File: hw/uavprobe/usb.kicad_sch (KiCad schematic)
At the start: 50 parts, among them J1 USB_C_Receptacle_USB2.0_14P, SW2 Reset, U6 NCP1117-5.0_SOT223, U7 TPS2561, U8 USB2412-DZK, Y2 24MHz

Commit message: AISLER-friendly BOM fields
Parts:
- J1: MPN USB4105-GF-A -> USB4105-GF-A
- SW2: MPN SW_SPST_B3U-1000P -> B3U-1000PM
- TP6, TP7, TP8, TP9: now left out of the parts list
- U6: MPN NCP1117-5.0_SOT223 -> NCP1117ST33T3G
- U7: MPN TPS2561 -> TPS2561DRCT
- Y2: MPN ABM3B-24.000MHZ-10-B-1-U-T -> ABM3B-24.000MHZ-10-1-U-T
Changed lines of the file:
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@@
 			)
 		)
-		(property "MPN" "SW_SPST_B3U-1000P"
+		(property "MPN" "B3U-1000PM"
 			(at 160.02 144.78 0)
 			(effects
@@
 		(unit 1)
 		(exclude_from_sim no)
-		(in_bom yes)
+		(in_bom no)
 		(on_board yes)
 		(dnp no)
@@
 		(unit 1)
 		(exclude_from_sim no)
-		(in_bom yes)
+		(in_bom no)
 		(on_board yes)
 		(dnp no)
@@
 		(unit 1)
 		(exclude_from_sim no)
-		(in_bom yes)
+		(in_bom no)
 		(on_board yes)
 		(dnp no)
@@
 			)
 		)
-		(property "MPN" "NCP1117-5.0_SOT223"
+		(property "MPN" "NCP1117ST33T3G"
 			(at 90.17 130.81 0)
 			(effects
@@
 			)
 		)
-		(property "MPN" "TPS2561"
+		(property "MPN" "TPS2561DRCT"
 			(at 83.82 168.91 0)
 			(effects
@@
 			)
 		)
-		(property "MPN" "USB4105-GF-A"
+		(property "MPN" "USB4105-GF-A "
 			(at 38.1 71.12 0)
 			(effects
@@
 		(unit 1)
 		(exclude_from_sim no)
-		(in_bom yes)
+		(in_bom no)
 		(on_board yes)
 		(dnp no)
@@
 			)
 		)
-		(property "MPN" "ABM3B-24.000MHZ-10-B-1-U-T"
+		(property "MPN" "ABM3B-24.000MHZ-10-1-U-T"
 			(at 194.31 52.07 0)
 			(effects

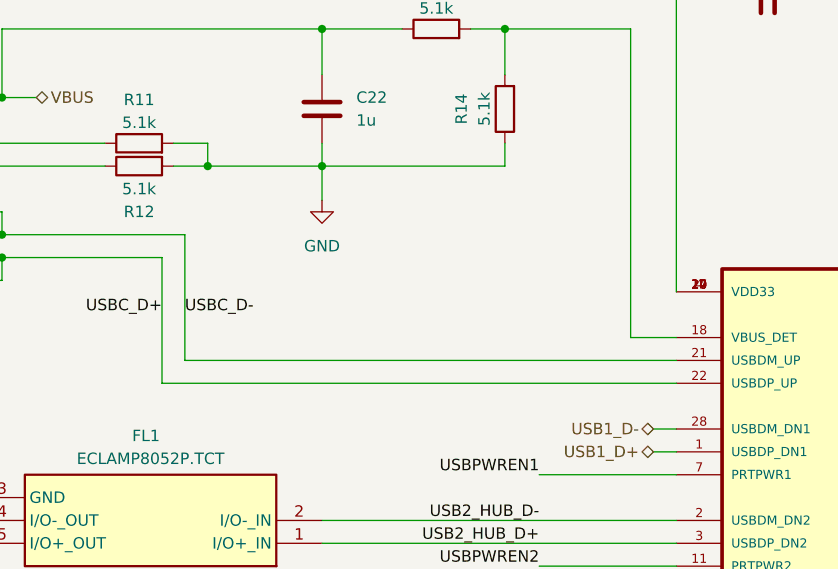
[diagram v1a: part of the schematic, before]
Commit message: Layout 2
Honoring the DRC and with a new uSB-C connector
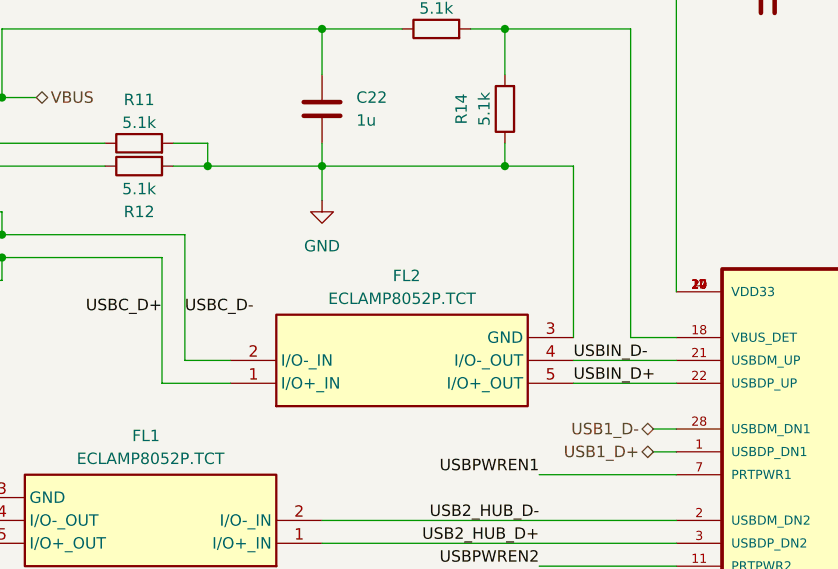
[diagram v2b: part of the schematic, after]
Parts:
- added FL2: ECLAMP8052P.TCT, Import:ECLAMP8052PTCT, symbol ECLAMP850:ECLAMP8052P.TCT
- J1: footprint Connector_USB:USB_C_Receptacle_GCT_USB4105-xx-A_16P_TopMnt_Horizontal -> Connector_USB:USB_C_Receptacle_Amphenol_124019772112A
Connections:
- net GND: now also FL2.3 (GND)
- net USBC_D+: now also FL2.1 (I/O+_IN); no longer U8.22 (USBDP_UP)
- net USBC_D-: now also FL2.2 (I/O-_IN); no longer U8.21 (USBDM_UP)
- new net USBIN_D+: FL2.5 (I/O+_OUT), U8.22 (USBDP_UP)
- new net USBIN_D-: FL2.4 (I/O-_OUT), U8.21 (USBDM_UP)
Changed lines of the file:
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@@
 	)
 	(junction
+		(at 114.3 63.5)
+		(diameter 0)
+		(color 0 0 0 0)
+	)
+	(junction
 		(at 110.49 149.86)
 		(diameter 0)
@@
 	(wire
 		(pts
+			(xy 121.92 85.09) (xy 133.35 85.09)
+		)
+		(stroke
+			(width 0)
+			(type default)
+		)
+	)
+	(wire
+		(pts
 			(xy 238.76 46.99) (xy 238.76 68.58)
 		)
@@
 	(wire
 		(pts
+			(xy 121.92 63.5) (xy 114.3 63.5)
+		)
+		(stroke
+			(width 0)
+			(type default)
+		)
+	)
+	(wire
+		(pts
 			(xy 199.39 67.31) (xy 199.39 77.47)
 		)
@@
 	(wire
 		(pts
-			(xy 252.73 116.84) (xy 261.62 116.84)
+			(xy 121.92 82.55) (xy 121.92 63.5)
 		)
 		(stroke
@@
 	(wire
 		(pts
-			(xy 53.34 63.5) (xy 69.85 63.5)
+			(xy 252.73 116.84) (xy 261.62 116.84)
 		)
 		(stroke
@@
 	(wire
 		(pts
-			(xy 210.82 44.45) (xy 210.82 57.15)
+			(xy 53.34 63.5) (xy 69.85 63.5)
 		)
 		(stroke
@@
 	(wire
 		(pts
-			(xy 93.98 60.96) (xy 93.98 63.5)
+			(xy 210.82 44.45) (xy 210.82 57.15)
 		)
 		(stroke
@@
 	(wire
 		(pts
-			(xy 114.3 63.5) (xy 114.3 60.96)
+			(xy 93.98 60.96) (xy 93.98 63.5)
 		)
 		(stroke
@@
 	(wire
 		(pts
-			(xy 110.49 158.75) (xy 123.19 158.75)
+			(xy 114.3 63.5) (xy 114.3 60.96)
 		)
 		(stroke
@@
 	(wire
 		(pts
-			(xy 133.35 85.09) (xy 78.74 85.09)
+			(xy 110.49 158.75) (xy 123.19 158.75)
 		)
 		(stroke
@@
 	(wire
 		(pts
-			(xy 76.2 87.63) (xy 133.35 87.63)
+			(xy 130.81 92.71) (xy 133.35 92.71)
 		)
 		(stroke
@@
 	(wire
 		(pts
-			(xy 130.81 92.71) (xy 133.35 92.71)
+			(xy 76.2 87.63) (xy 83.82 87.63)
 		)
 		(stroke
@@
 	(wire
 		(pts
+			(xy 78.74 85.09) (xy 83.82 85.09)
+		)
+		(stroke
+			(width 0)
+			(type default)
+		)
+	)
+	(wire
+		(pts
 			(xy 245.11 68.58) (xy 238.76 68.58)
 		)
@@
 		)
 	)
+	(wire
+		(pts
+			(xy 121.92 87.63) (xy 133.35 87.63)
+		)
+		(stroke
+			(width 0)
+			(type default)
+		)
+	)
 	(label "~{RESET}"
 		(at 182.88 151.13 0)
@@
 		)
 	)
+	(label "USBIN_D-"
+		(at 121.92 85.09 0)
+		(effects
+			(font
+				(size 1.27 1.27)
+			)
+			(justify left bottom)
+		)
+	)
+	(label "USBIN_D+"
+		(at 121.92 87.63 0)
+		(effects
+			(font
+				(size 1.27 1.27)
+			)
+			(justify left bottom)
+		)
+	)
 	(label "FAULT2"
 		(at 275.59 80.01 0)
@@
 	)
 	(symbol
+		(lib_id "ECLAMP850:ECLAMP8052P.TCT")
+		(at 83.82 87.63 0)
+		(mirror x)
+		(unit 1)
+		(exclude_from_sim no)
+		(in_bom yes)
+		(on_board yes)
+		(dnp no)
+		(property "Reference" "FL2"
+			(at 103.378 75.692 0)
+			(effects
+				(font
+					(size 1.27 1.27)
+				)
+			)
+		)
+		(property "Value" "ECLAMP8052P.TCT"
+			(at 102.87 78.232 0)
+			(effects
+				(font
+					(size 1.27 1.27)
+				)
+			)
+		)
+		(property "Footprint" "Import:ECLAMP8052PTCT"
+			(at 118.11 -7.29 0)
+			(effects
+				(font
+					(size 1.27 1.27)
+				)
+				(justify left top)
+				(hide yes)
+			)
+		)
+		(property "Datasheet" "https://semtech.my.salesforce.com/sfc/p/#E0000000JelG/a/44000000MClt/x4_O.M8f1_5l6CovuR7Nj9RxqDFB_sAgVeqN73g7pps"
+			(at 118.11 -107.29 0)
+			(effects
+				(font
+					(size 1.27 1.27)
+				)
+				(justify left top)
+				(hide yes)
+			)
+		)
+		(property "Description" "ESD Suppressors / TVS Diodes COMMON MODE FILTER & ESD"
+			(at 83.82 87.63 0)
+			(effects
+				(font
+					(size 1.27 1.27)
+				)
+				(hide yes)
+			)
+		)
+		(property "Height" "0.6"
+			(at 118.11 -307.29 0)
+			(effects
+				(font
+					(size 1.27 1.27)
+				)
+				(justify left top)
+				(hide yes)
+			)
+		)
+		(property "Manufacturer_Name" "SEMTECH"
+			(at 118.11 -407.29 0)
+			(effects
+				(font
+					(size 1.27 1.27)
+				)
+				(justify left top)
+				(hide yes)
+			)
+		)
+		(property "MPN" "ECLAMP8052P.TCT"
+			(at 118.11 -507.29 0)
+			(effects
+				(font
+					(size 1.27 1.27)
+				)
+				(justify left top)
+				(hide yes)
+			)
+		)
+		(property "Mouser Part Number" "947-ECLAMP8052P.TCT"
+			(at 118.11 -607.29 0)
+			(effects
+				(font
+					(size 1.27 1.27)
+				)
+				(justify left top)
+				(hide yes)
+			)
+		)
+		(property "Mouser Price/Stock" "https://www.mouser.co.uk/ProductDetail/Semtech/ECLAMP8052P.TCT?qs=rBWM4%252BvDhIdksQ1MWttwUQ%3D%3D"
+			(at 118.11 -707.29 0)
+			(effects
+				(font
+					(size 1.27 1.27)
+				)
+				(justify left top)
+				(hide yes)
+			)
+		)
+		(property "Arrow Part Number" "ECLAMP8052P.TCT"
+			(at 118.11 -807.29 0)
+			(effects
+				(font
+					(size 1.27 1.27)
+				)
+				(justify left top)
+				(hide yes)
+			)
+		)
+		(property "Arrow Price/Stock" "https://www.arrow.com/en/products/eclamp8052p.tct/semtech?region=nac"
+			(at 118.11 -907.29 0)
+			(effects
+				(font
+					(size 1.27 1.27)
+				)
+				(justify left top)
+				(hide yes)
+			)
+		)
+		(property "MP" ""
+			(at 83.82 87.63 0)
+			(effects
+				(font
+					(size 1.27 1.27)
+				)
+				(hide yes)
+			)
+		)
+		(property "Manufacturer_Part_Number" ""
+			(at 83.82 87.63 0)
+			(effects
+				(font
+					(size 1.27 1.27)
+				)
+				(hide yes)
+			)
+		)
+		(pin "1"
+		)
+		(pin "2"
+		)
+		(pin "5"
+		)
+		(pin "3"
+		)
+		(pin "4"
+		)
+		(instances
+			(project "uavprobe"
+				(path "/e4efab0a-eb38-47b4-a7c8-7fdbedea4819/199cf35c-4212-4d48-8fab-6a59511a8aed"
+					(reference "FL2")
+					(unit 1)
+				)
+			)
+		)
+	)
+	(symbol
 		(lib_id "power:GND")
 		(at 30.48 109.22 0)
@@
 			)
 		)
-		(property "Footprint" "Connector_USB:USB_C_Receptacle_GCT_USB4105-xx-A_16P_TopMnt_Horizontal"
+		(property "Footprint" "Connector_USB:USB_C_Receptacle_Amphenol_124019772112A"
 			(at 41.91 71.12 0)
 			(effects

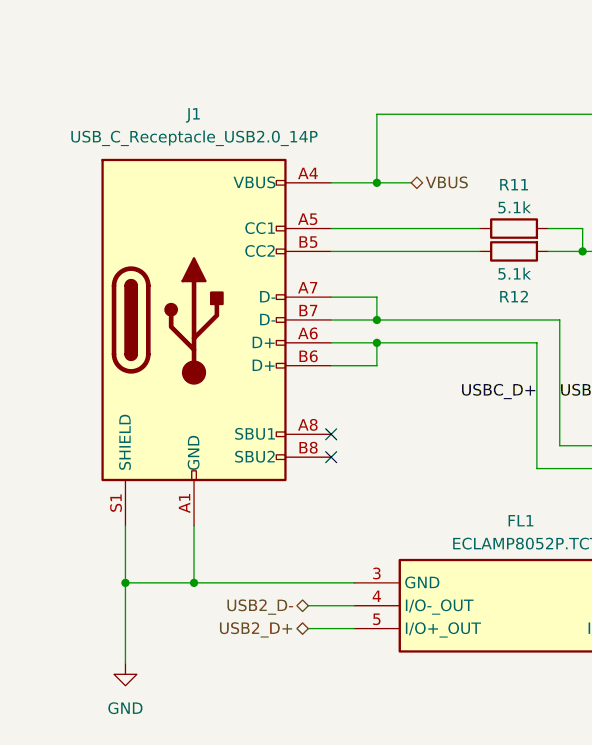
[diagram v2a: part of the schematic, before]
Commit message: USB-C connector change
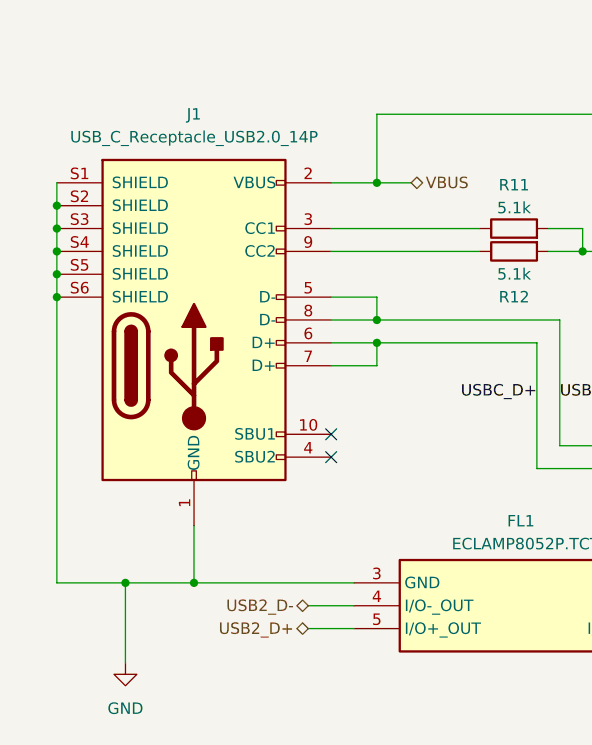
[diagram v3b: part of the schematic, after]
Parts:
- J1: footprint Connector_USB:USB_C_Receptacle_Amphenol_124019772112A -> Import:JAE_DX07S016JA1R1500; MPN USB4105-GF-A -> DX07S016JA1R1500
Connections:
- net GND: now also J1.1 (GND), J1.12 (GND), J1.S2 (SHIELD), J1.S3 (SHIELD), J1.S4 (SHIELD), J1.S5 (SHIELD), J1.S6 (SHIELD); no longer J1.A1 (GND), J1.A12 (GND), J1.B1 (GND), J1.B12 (GND)
- net USBC_D+: now also J1.6 (D+), J1.7 (D+); no longer J1.A6 (D+), J1.B6 (D+)
- net USBC_D-: now also J1.5 (D-), J1.8 (D-); no longer J1.A7 (D-), J1.B7 (D-)
- net VBUS: now also J1.11 (VBUS), J1.2 (VBUS); no longer J1.A4 (VBUS), J1.A9 (VBUS), J1.B4 (VBUS), J1.B9 (VBUS)
- net at R12.1: now also J1.9 (CC2); no longer J1.B5 (CC2)
- net at R11.1: now also J1.3 (CC1); no longer J1.A5 (CC1)
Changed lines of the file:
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@@
 	)
 	(junction
+		(at 22.86 63.5)
+		(diameter 0)
+		(color 0 0 0 0)
+	)
+	(junction
 		(at 93.98 63.5)
 		(diameter 0)
@@
 	)
 	(junction
+		(at 22.86 68.58)
+		(diameter 0)
+		(color 0 0 0 0)
+	)
+	(junction
 		(at 129.54 138.43)
 		(diameter 0)
@@
 	)
 	(junction
+		(at 22.86 58.42)
+		(diameter 0)
+		(color 0 0 0 0)
+	)
+	(junction
 		(at 93.98 48.26)
 		(diameter 0)
@@
 	)
 	(junction
+		(at 22.86 60.96)
+		(diameter 0)
+		(color 0 0 0 0)
+	)
+	(junction
+		(at 22.86 66.04)
+		(diameter 0)
+		(color 0 0 0 0)
+	)
+	(junction
 		(at 114.3 48.26)
 		(diameter 0)
@@
 	(wire
 		(pts
+			(xy 22.86 63.5) (xy 22.86 66.04)
+		)
+		(stroke
+			(width 0)
+			(type default)
+		)
+	)
+	(wire
+		(pts
 			(xy 199.39 67.31) (xy 199.39 77.47)
 		)
@@
 	(wire
 		(pts
-			(xy 30.48 93.98) (xy 30.48 100.33)
+			(xy 22.86 68.58) (xy 22.86 100.33)
 		)
 		(stroke
@@
 	(wire
 		(pts
+			(xy 22.86 55.88) (xy 22.86 58.42)
+		)
+		(stroke
+			(width 0)
+			(type default)
+		)
+	)
+	(wire
+		(pts
 			(xy 147.32 44.45) (xy 194.31 44.45)
 		)
@@
 	(wire
 		(pts
+			(xy 22.86 60.96) (xy 22.86 63.5)
+		)
+		(stroke
+			(width 0)
+			(type default)
+		)
+	)
+	(wire
+		(pts
 			(xy 238.76 80.01) (xy 245.11 80.01)
 		)
@@
 	(wire
 		(pts
+			(xy 22.86 58.42) (xy 22.86 60.96)
+		)
+		(stroke
+			(width 0)
+			(type default)
+		)
+	)
+	(wire
+		(pts
 			(xy 104.14 125.73) (xy 104.14 130.81)
 		)
@@
 	(wire
 		(pts
+			(xy 22.86 100.33) (xy 30.48 100.33)
+		)
+		(stroke
+			(width 0)
+			(type default)
+		)
+	)
+	(wire
+		(pts
 			(xy 93.98 105.41) (xy 133.35 105.41)
 		)
@@
 	(wire
 		(pts
+			(xy 22.86 66.04) (xy 22.86 68.58)
+		)
+		(stroke
+			(width 0)
+			(type default)
+		)
+	)
+	(wire
+		(pts
 			(xy 190.5 90.17) (xy 184.15 90.17)
 		)
@@
 			)
 		)
-		(property "Footprint" "Connector_USB:USB_C_Receptacle_Amphenol_124019772112A"
+		(property "Footprint" "Import:JAE_DX07S016JA1R1500"
 			(at 41.91 71.12 0)
 			(effects
@@
 			)
 		)
-		(property "MPN" "USB4105-GF-A "
+		(property "MPN" "DX07S016JA1R1500"
 			(at 38.1 71.12 0)
 			(effects
@@
 			)
 		)
-		(pin "B7"
+		(pin "4"
 		)
-		(pin "B1"
+		(pin "S4"
 		)
-		(pin "B5"
+		(pin "10"
 		)
-		(pin "A12"
+		(pin "1"
 		)
-		(pin "A4"
+		(pin "S3"
 		)
-		(pin "B6"
+		(pin "7"
 		)
 		(pin "S1"
 		)
-		(pin "A9"
+		(pin "S5"
 		)
-		(pin "B9"
+		(pin "12"
 		)
-		(pin "B12"
+		(pin "2"
 		)
-		(pin "A1"
+		(pin "S2"
+		)
+		(pin "8"
 		)
-		(pin "A5"
+		(pin "9"
 		)
-		(pin "A6"
+		(pin "5"
 		)
-		(pin "A7"
+		(pin "S6"
 		)
-		(pin "B4"
+		(pin "6"
 		)
-		(pin "A8"
+		(pin "3"
 		)
-		(pin "B8"
+		(pin "11"
 		)
 		(instances

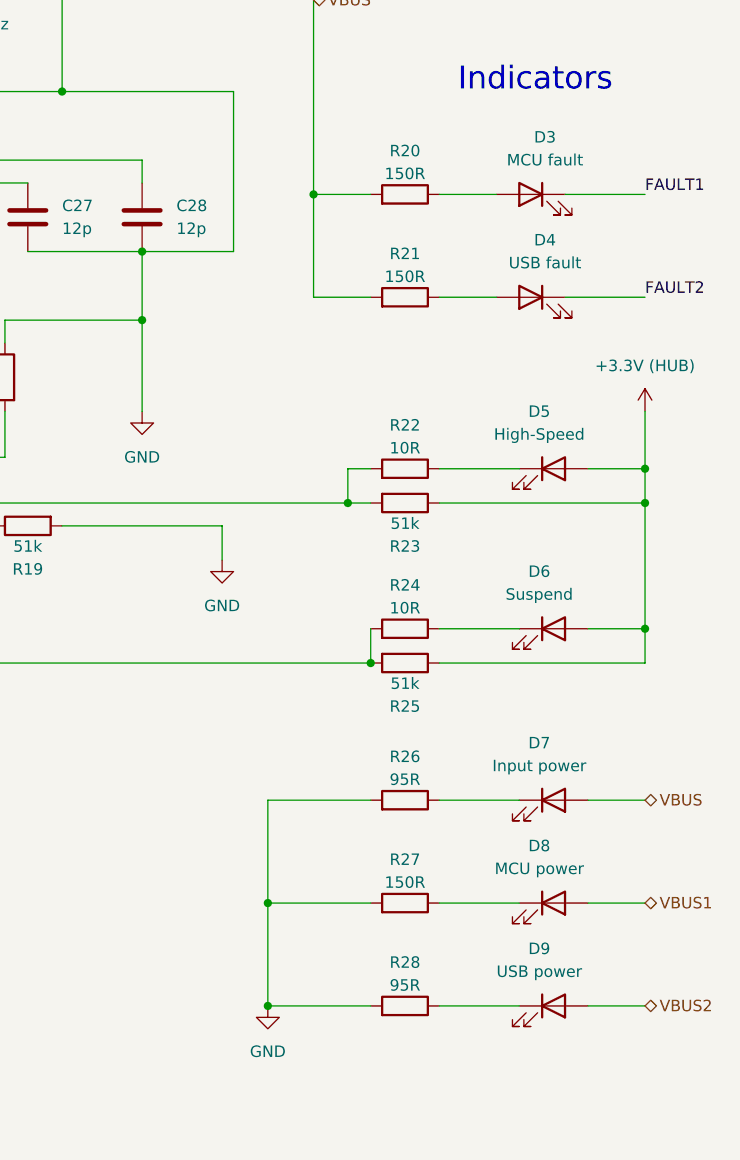
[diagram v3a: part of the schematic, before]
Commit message: LEDs reconfigured for 10 mA current
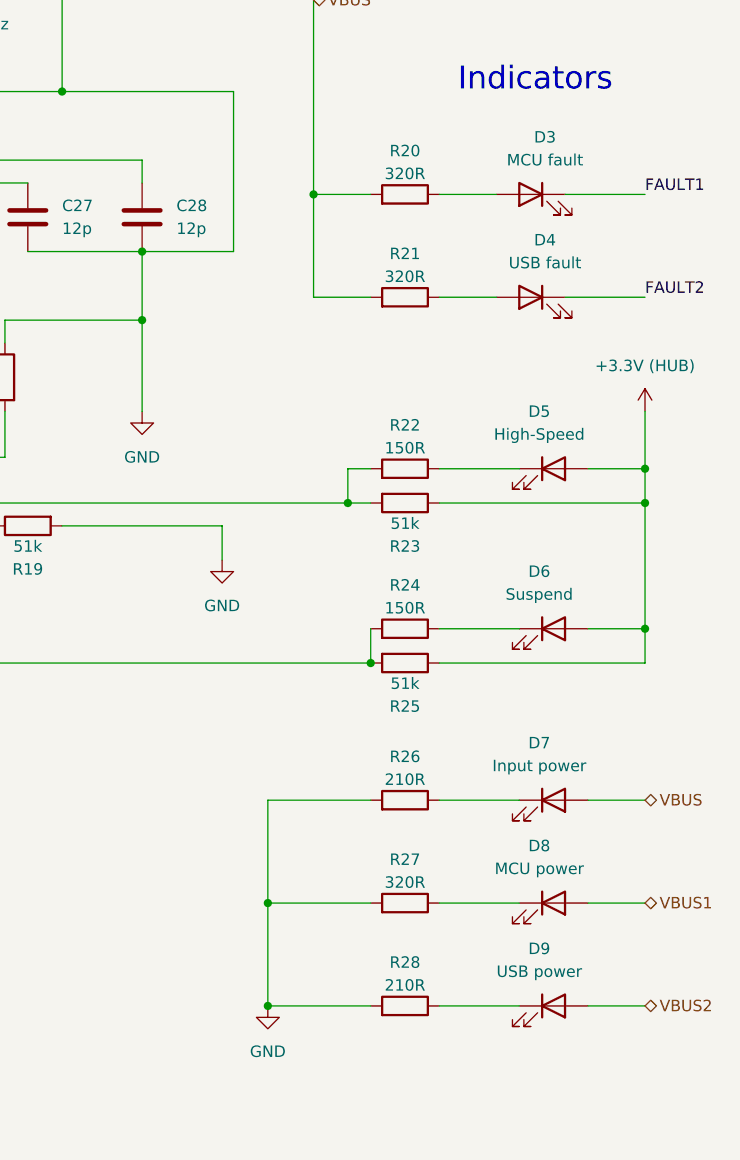
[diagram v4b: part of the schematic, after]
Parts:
- R20, R21, R27: value 150R -> 320R
- R22, R24: value 10R -> 150R
- R26, R28: value 95R -> 210R
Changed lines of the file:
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@@
 		(on_board yes)
 		(dnp no)
+		(fields_autoplaced yes)
 		(property "Reference" "D3"
 			(at 264.4775 62.23 0)
@@
 		(on_board yes)
 		(dnp no)
+		(fields_autoplaced yes)
 		(property "Reference" "R18"
 			(at 199.644 88.9 90)
@@
 		(on_board yes)
 		(dnp no)
+		(fields_autoplaced yes)
 		(property "Reference" "R26"
 			(at 248.92 131.064 90)
@@
 			)
 		)
-		(property "Value" "95R"
+		(property "Value" "210R"
 			(at 248.92 133.604 90)
 			(effects
@@
 		(on_board yes)
 		(dnp no)
+		(fields_autoplaced yes)
 		(property "Reference" "R20"
 			(at 248.92 63.754 90)
@@
 			)
 		)
-		(property "Value" "150R"
+		(property "Value" "320R"
 			(at 248.92 66.294 90)
 			(effects
@@
 		(on_board yes)
 		(dnp no)
+		(fields_autoplaced yes)
 		(property "Reference" "R23"
 			(at 248.92 107.696 90)
@@
 		(on_board yes)
 		(dnp no)
+		(fields_autoplaced yes)
 		(property "Reference" "R17"
 			(at 194.31 72.644 90)
@@
 		(on_board yes)
 		(dnp no)
+		(fields_autoplaced yes)
 		(property "Reference" "C24"
 			(at 110.49 123.1899 0)
@@
 		(on_board yes)
 		(dnp no)
+		(fields_autoplaced yes)
 		(property "Reference" "R21"
 			(at 248.92 75.184 90)
@@
 			)
 		)
-		(property "Value" "150R"
+		(property "Value" "320R"
 			(at 248.92 77.724 90)
 			(effects
@@
 		(on_board yes)
 		(dnp no)
+		(fields_autoplaced yes)
 		(property "Reference" "R22"
 			(at 248.92 94.234 90)
@@
 			)
 		)
-		(property "Value" "10R"
+		(property "Value" "150R"
 			(at 248.92 96.774 90)
 			(effects
@@
 		(on_board yes)
 		(dnp no)
+		(fields_autoplaced yes)
 		(property "Reference" "R10"
 			(at 63.754 180.34 90)
@@
 		(on_board yes)
 		(dnp no)
+		(fields_autoplaced yes)
 		(property "Reference" "FL1"
 			(at 74.422 93.472 0)
@@
 		(on_board yes)
 		(dnp no)
+		(fields_autoplaced yes)
 		(property "Reference" "TP8"
 			(at 26.67 158.4324 0)
@@
 		(on_board yes)
 		(dnp no)
+		(fields_autoplaced yes)
 		(property "Reference" "R28"
 			(at 248.92 153.924 90)
@@
 			)
 		)
-		(property "Value" "95R"
+		(property "Value" "210R"
 			(at 248.92 156.464 90)
 			(effects
@@
 		(on_board yes)
 		(dnp no)
+		(fields_autoplaced yes)
 		(property "Reference" "R16"
 			(at 185.42 139.954 90)
@@
 		(on_board yes)
 		(dnp no)
+		(fields_autoplaced yes)
 		(property "Reference" "R24"
 			(at 248.92 112.014 90)
@@
 			)
 		)
-		(property "Value" "10R"
+		(property "Value" "150R"
 			(at 248.92 114.554 90)
 			(effects
@@
 		(on_board yes)
 		(dnp no)
+		(fields_autoplaced yes)
 		(property "Reference" "R15"
 			(at 170.18 149.606 90)
@@
 		(on_board yes)
 		(dnp no)
+		(fields_autoplaced yes)
 		(property "Reference" "TP9"
 			(at 26.67 166.0524 0)
@@
 		(on_board yes)
 		(dnp no)
+		(fields_autoplaced yes)
 		(property "Reference" "R12"
 			(at 73.66 68.58 90)
@@
 		(on_board yes)
 		(dnp no)
+		(fields_autoplaced yes)
 		(property "Reference" "R13"
 			(at 106.68 43.434 90)
@@
 		(on_board yes)
 		(dnp no)
+		(fields_autoplaced yes)
 		(property "Reference" "R19"
 			(at 207.01 110.236 90)
@@
 		(on_board yes)
 		(dnp no)
+		(fields_autoplaced yes)
 		(property "Reference" "U8"
 			(at 158.75 69.85 0)
@@
 		(on_board yes)
 		(dnp no)
+		(fields_autoplaced yes)
 		(property "Reference" "FL2"
 			(at 103.378 75.692 0)
@@
 		(on_board yes)
 		(dnp no)
+		(fields_autoplaced yes)
 		(property "Reference" "C25"
 			(at 123.19 123.1899 0)
@@
 		(on_board yes)
 		(dnp no)
+		(fields_autoplaced yes)
 		(property "Reference" "R14"
 			(at 109.474 57.15 90)
@@
 		(on_board yes)
 		(dnp no)
+		(fields_autoplaced yes)
 		(property "Reference" "TP7"
 			(at 26.67 150.8124 0)
@@
 		(on_board yes)
 		(dnp no)
+		(fields_autoplaced yes)
 		(property "Reference" "R27"
 			(at 248.92 142.494 90)
@@
 			)
 		)
-		(property "Value" "150R"
+		(property "Value" "320R"
 			(at 248.92 145.034 90)
 			(effects
@@
 		(on_board yes)
 		(dnp no)
+		(fields_autoplaced yes)
 		(property "Reference" "U6"
 			(at 90.17 124.46 0)
@@
 		(on_board yes)
 		(dnp no)
+		(fields_autoplaced yes)
 		(property "Reference" "U7"
 			(at 83.82 153.67 0)
@@
 		(on_board yes)
 		(dnp no)
+		(fields_autoplaced yes)
 		(property "Reference" "R11"
 			(at 73.66 56.134 90)
@@
 		(on_board yes)
 		(dnp no)
+		(fields_autoplaced yes)
 		(property "Reference" "TP6"
 			(at 26.67 143.1924 0)
@@
 		(on_board yes)
 		(dnp no)
+		(fields_autoplaced yes)
 		(property "Reference" "R25"
 			(at 248.92 125.476 90)
@@
 		(on_board yes)
 		(dnp no)
+		(fields_autoplaced yes)
 		(property "Reference" "D4"
 			(at 264.4775 73.66 0)
